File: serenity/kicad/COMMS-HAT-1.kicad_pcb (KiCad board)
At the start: 4 copper layers, 65 x 48 mm, 25 parts, among them J1 JST-GH-4P, J2 JST-GH-6P, J3 JST-GH-6P, J4 JST-GH-4P, Y1 25MHz

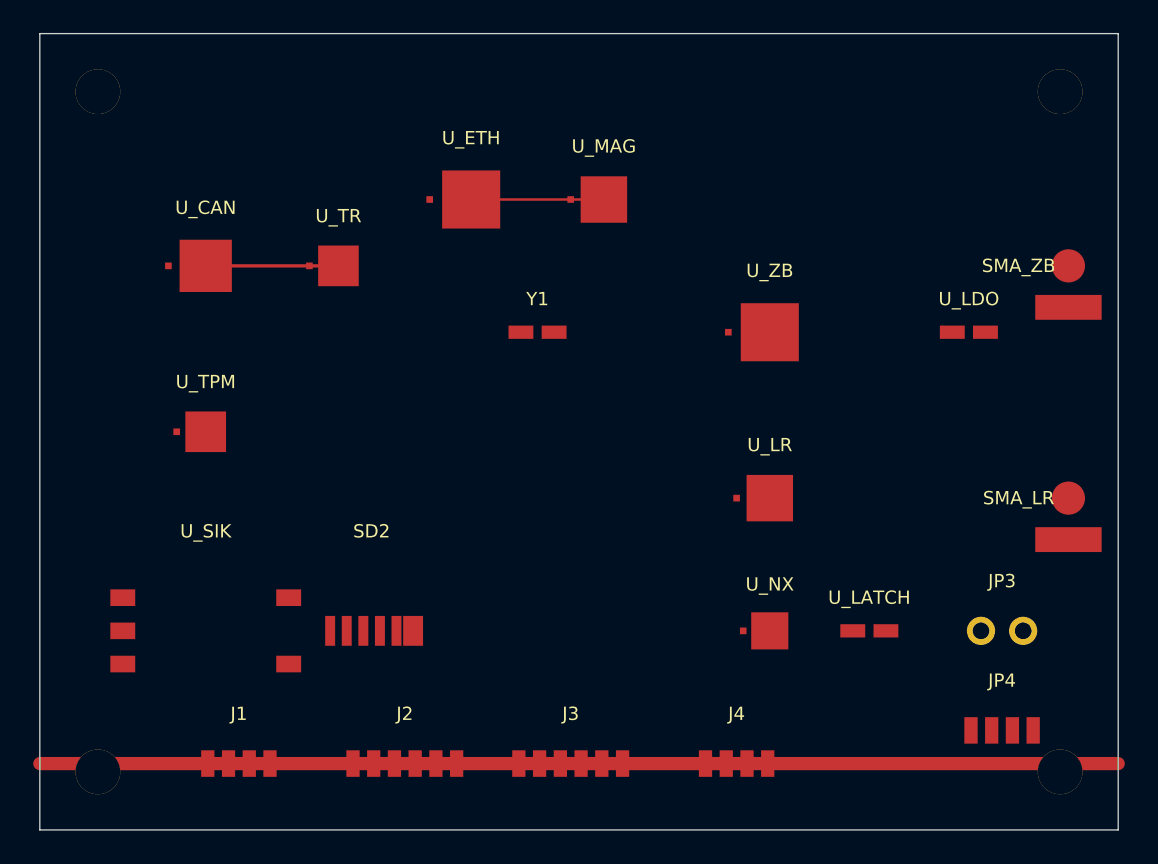
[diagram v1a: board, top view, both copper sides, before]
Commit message: Replace generic PCB silk labels with short descriptive names
Update all F.SilkS/B.SilkS fp_text reference labels across 7 KiCad PCB
files, replacing J/U/T numeric designators with function-based names so
each component is identifiable on the board without a BOM lookup.

CAPE-A-1 / CAPE-A-1-no-comment:
  J1→PB2-P1, J2→PB2-P2, U1→IMU, U2→BARO, U3→GPS,
  U4/U5→CAN-TR/RS485, U6→1553-DRV, U7→1553-RCV, T1→1553-XFM,
  U8/U9→ETH1-PHY/ETH2-PHY, U10→TPM,
  J3→CAN-FD, J4→RS-485, J5→MIL-1553, J6→ETH1, J7→ETH2,
  J8→ESC-TLM, J9→SERVO, J10→PWR-IN

CAPE-B-1 (adds RF + payload peripherals):
  U1→LORA, U2→WIFI-BT, U10→SD-WB, U11→NOR-FLASH,
  U12→WINCH-DRV, U13→LOAD-ADC, U14→PWM-I2C,
  J8→SIK-TLM, J9→RC-RCVR, J11→WINCH, J12→LOAD-CELL, J13→NAV-LIGHT

COMMS-HAT-1 (connectors + crystal only; ICs already descriptive):
  J1→SIK-UART, J2→ETH, J3→GPIO-EXT, J4→CAN-FD,
  JP4→PWR-IN, Y1→ETH-CLK

COMMS-HAT-SWITCH:
  Y1→SW-CLK

TRIHAT-1 (superseded; ICs + inferred connector mapping):
  U1→IMU, U2→BARO, U3→GPS, U4→CAN-CTRL, U5→CAN-TR,
  U6→ETH-CTRL, U7→ETH-MAG, U8→TPM, U9→LDO, Y1→ETH-CLK,
  J-connectors mapped from net list (GPS/CAN-FD/ETH/ESC-OUT/SERVO-OUT/etc.)

CM3-CARRIER-1:
  J1→CM3-SDIMM, U1→CAN-CTRL, U1B→CAN-TR, U2→RS485,
  U3→MIL-1553, U4→ETH-CTRL, U5→USB-UART, U6→LDO, U7→HAT-EEPROM

Boards already fully descriptive (SENSORHAT-1, CM4-CARRIER-1,
CM4-CARRIER-2) are unchanged.

https://claude.ai/code/session_01GniMw4QukTVM7JMzyVjH6p
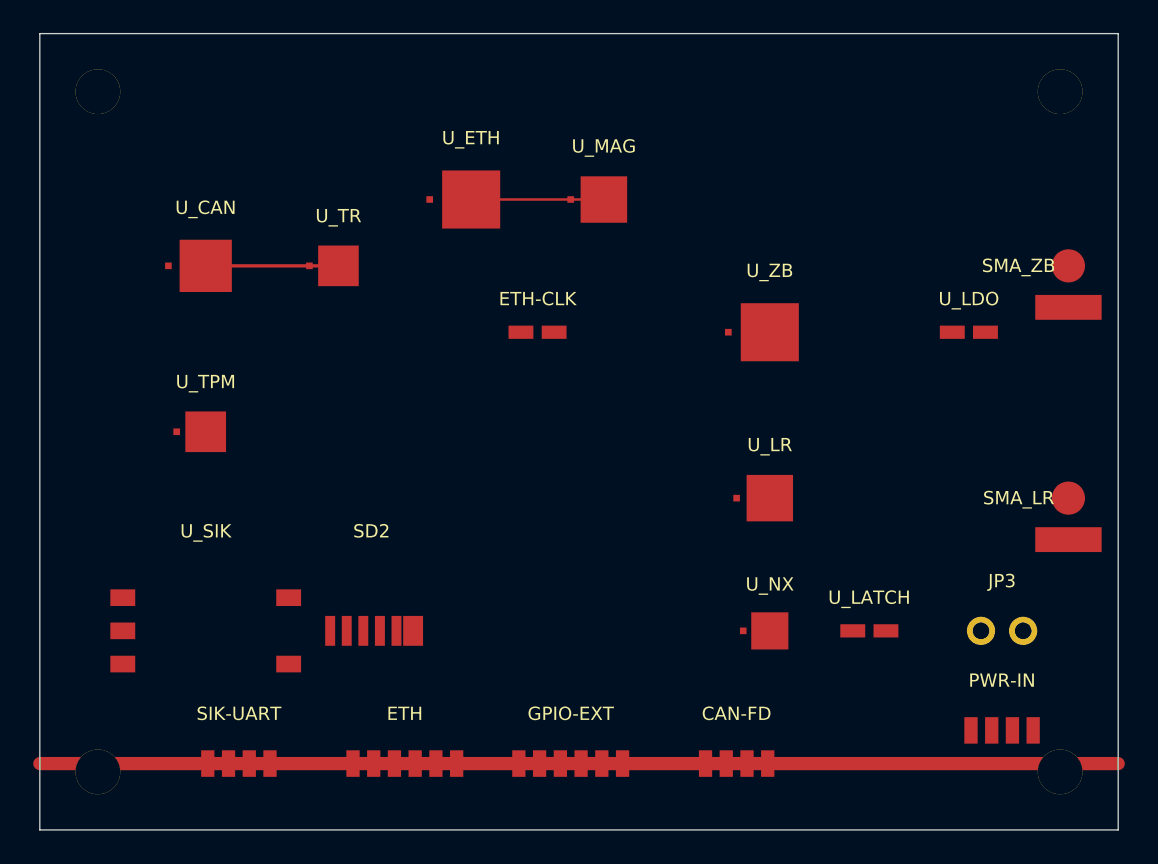
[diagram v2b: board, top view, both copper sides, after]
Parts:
- removed J1, J4, JP4: JST-GH-4P, Connector_JST:JST_GH_SM04B-GHS-TB_1x04_P1.25mm_Horizontal
- removed J2, J3: JST-GH-6P, Connector_JST:JST_GH_SM06B-GHS-TB_1x06_P1.25mm_Horizontal
- removed Y1: 25MHz, Crystal:Crystal_SMD_3225-4Pin_3.2x2.5mm
- added CAN-FD: JST-GH-4P, Connector_JST:JST_GH_SM04B-GHS-TB_1x04_P1.25mm_Horizontal, F.Cu at (42.0, 44.0)
- added ETH: JST-GH-6P, Connector_JST:JST_GH_SM06B-GHS-TB_1x06_P1.25mm_Horizontal, F.Cu at (22.0, 44.0)
- added ETH-CLK: 25MHz, Crystal:Crystal_SMD_3225-4Pin_3.2x2.5mm, F.Cu at (30.0, 18.0)
- added GPIO-EXT: JST-GH-6P, Connector_JST:JST_GH_SM06B-GHS-TB_1x06_P1.25mm_Horizontal, F.Cu at (32.0, 44.0)
- added PWR-IN: JST-GH-4P, Connector_JST:JST_GH_SM04B-GHS-TB_1x04_P1.25mm_Horizontal, F.Cu at (58.0, 42.0)
- added SIK-UART: JST-GH-4P, Connector_JST:JST_GH_SM04B-GHS-TB_1x04_P1.25mm_Horizontal, F.Cu at (12.0, 44.0)
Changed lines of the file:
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@@
     (at 30 18)
     (property "Description" "W5500 reference clock")
-    (fp_text reference "Y1" (at 0 -2) (layer "F.SilkS")
+    (fp_text reference "ETH-CLK" (at 0 -2) (layer "F.SilkS")
       (effects (font (size 0.8 0.8) (thickness 0.15))))
     (fp_text value "25MHz" (at 0 2) (layer "F.Fab")
@@
   (footprint "Connector_JST:JST_GH_SM04B-GHS-TB_1x04_P1.25mm_Horizontal" (layer "F.Cu")
     (at 58 42) (property "Description" "JST-GH 1.25mm 4-pin connector")
-    (fp_text reference "JP4" (at 0 -3) (layer "F.SilkS")
+    (fp_text reference "PWR-IN" (at 0 -3) (layer "F.SilkS")
       (effects (font (size 0.8 0.8) (thickness 0.15))))
     (fp_text value "JST-GH-4P" (at 0 3) (layer "F.Fab")
@@
   (footprint "Connector_JST:JST_GH_SM04B-GHS-TB_1x04_P1.25mm_Horizontal" (layer "F.Cu")
     (at 12 44) (property "Description" "JST-GH 1.25mm 4-pin connector")
-    (fp_text reference "J1" (at 0 -3) (layer "F.SilkS")
+    (fp_text reference "SIK-UART" (at 0 -3) (layer "F.SilkS")
       (effects (font (size 0.8 0.8) (thickness 0.15))))
     (fp_text value "JST-GH-4P" (at 0 3) (layer "F.Fab")
@@
   (footprint "Connector_JST:JST_GH_SM06B-GHS-TB_1x06_P1.25mm_Horizontal" (layer "F.Cu")
     (at 22 44) (property "Description" "JST-GH 1.25mm 6-pin connector")
-    (fp_text reference "J2" (at 0 -3) (layer "F.SilkS")
+    (fp_text reference "ETH" (at 0 -3) (layer "F.SilkS")
       (effects (font (size 0.8 0.8) (thickness 0.15))))
     (fp_text value "JST-GH-6P" (at 0 3) (layer "F.Fab")
@@
   (footprint "Connector_JST:JST_GH_SM06B-GHS-TB_1x06_P1.25mm_Horizontal" (layer "F.Cu")
     (at 32 44) (property "Description" "JST-GH 1.25mm 6-pin connector")
-    (fp_text reference "J3" (at 0 -3) (layer "F.SilkS")
+    (fp_text reference "GPIO-EXT" (at 0 -3) (layer "F.SilkS")
       (effects (font (size 0.8 0.8) (thickness 0.15))))
     (fp_text value "JST-GH-6P" (at 0 3) (layer "F.Fab")
@@
   (footprint "Connector_JST:JST_GH_SM04B-GHS-TB_1x04_P1.25mm_Horizontal" (layer "F.Cu")
     (at 42 44) (property "Description" "JST-GH 1.25mm 4-pin connector")
-    (fp_text reference "J4" (at 0 -3) (layer "F.SilkS")
+    (fp_text reference "CAN-FD" (at 0 -3) (layer "F.SilkS")
       (effects (font (size 0.8 0.8) (thickness 0.15))))
     (fp_text value "JST-GH-4P" (at 0 3) (layer "F.Fab")
